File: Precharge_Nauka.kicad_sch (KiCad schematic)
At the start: 60 parts, among them Q1 C2M0280120D, Q2 C2M0280120D, Q3 C2M0280120D, Q4 2N7002, Q5 C2M0280120D, U32 LMV321

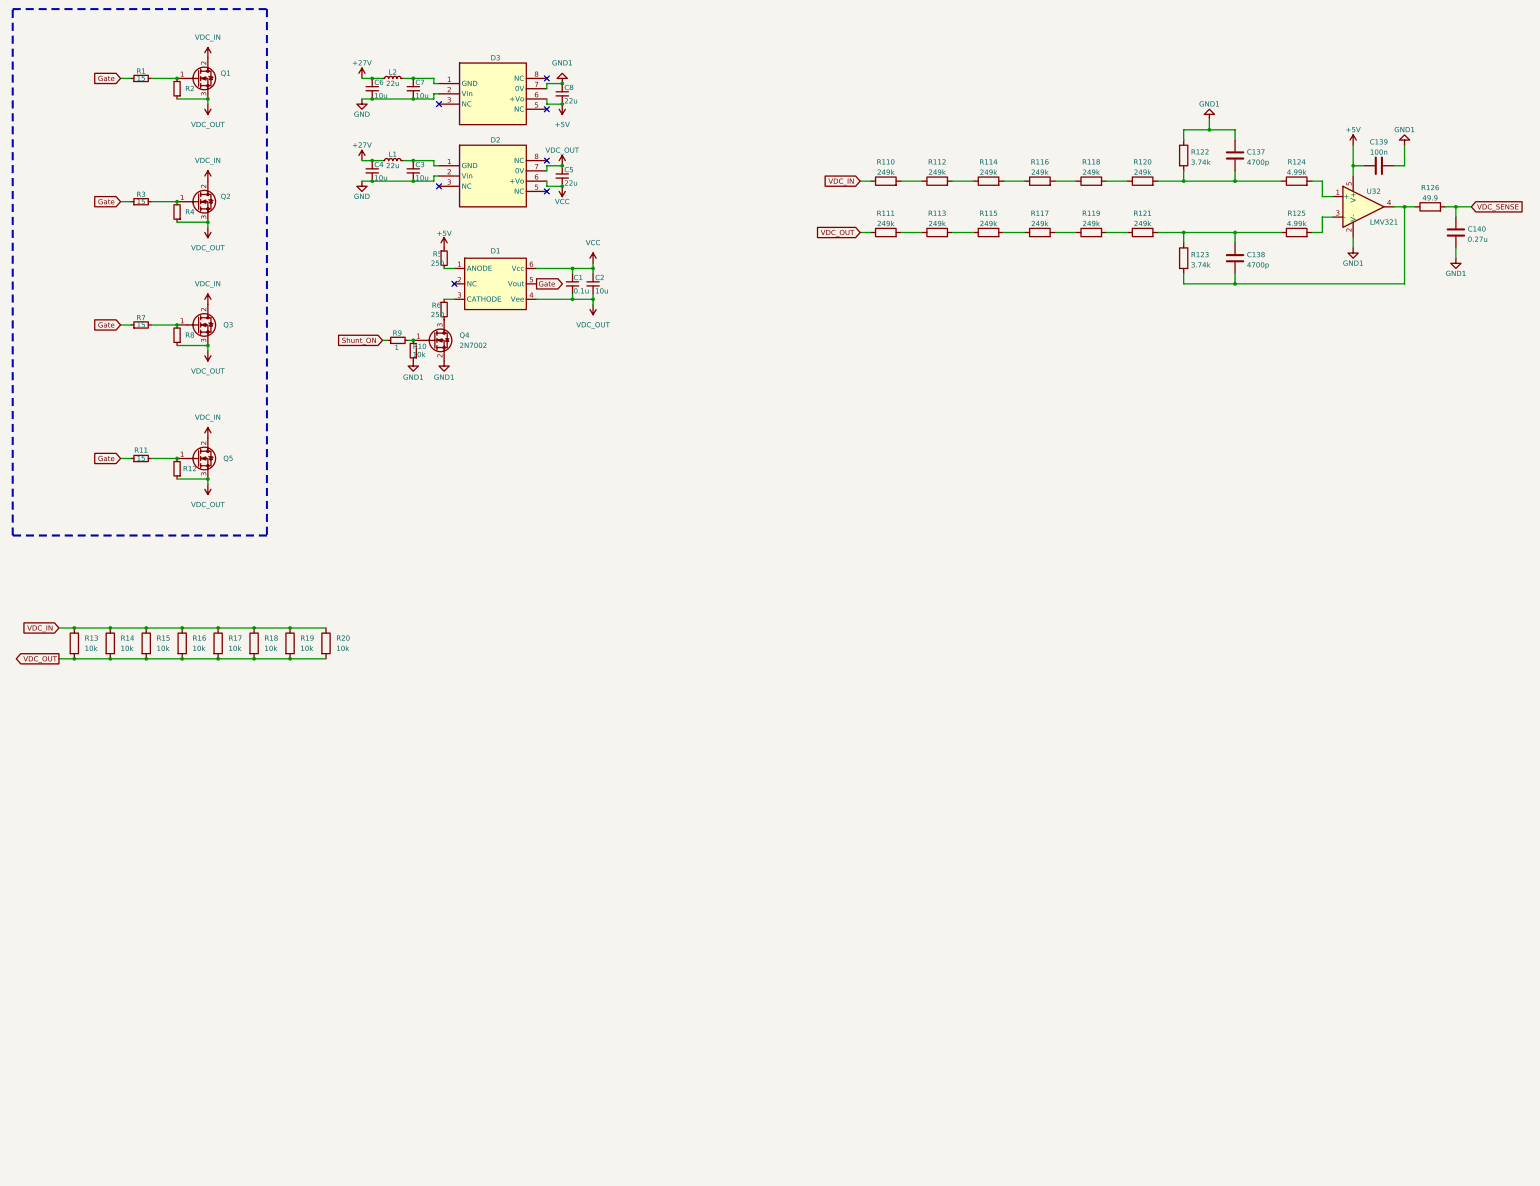
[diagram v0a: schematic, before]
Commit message: VER1.0: закончил основную схему и раскидал на плате
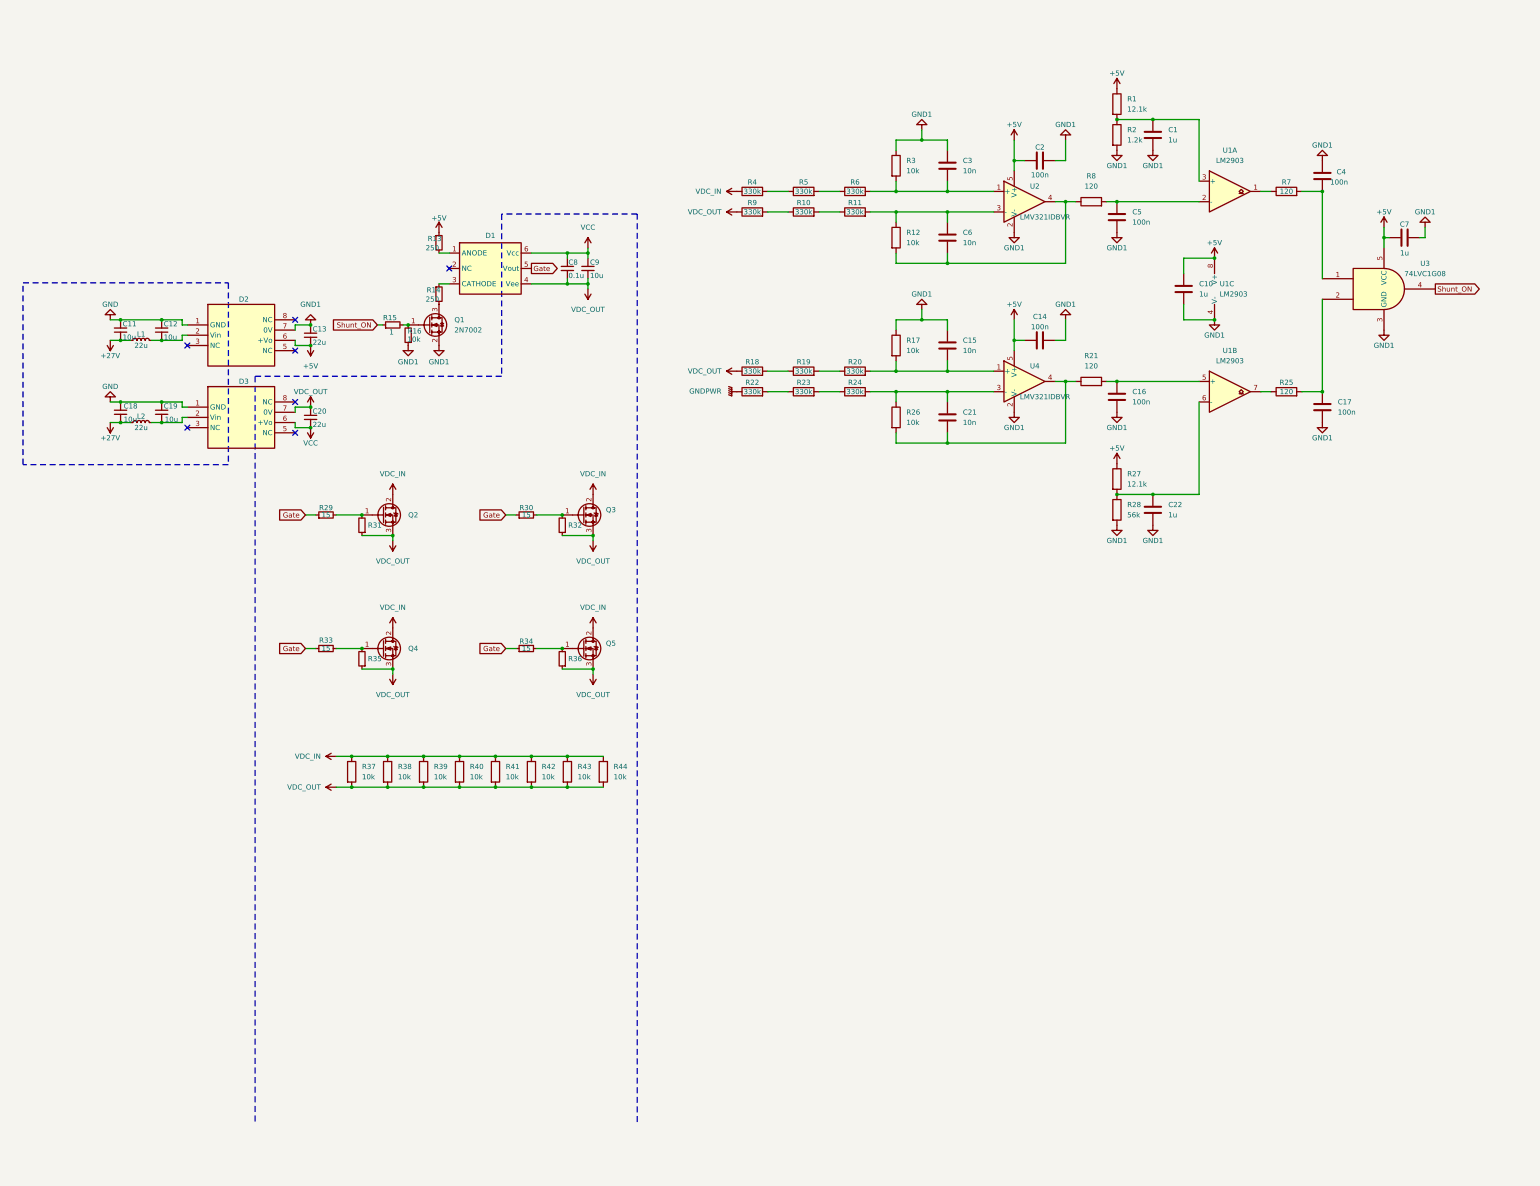
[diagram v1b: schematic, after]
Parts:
- removed R110, R111, R112, R113, R114, R115: 249k, Resistor_SMD:R_1206_3216Metric, symbol Device:R
- removed R124, R125: 4.99k, Resistor_SMD:R_0603_1608Metric, symbol Device:R
- added C1, C10, C22, C7: 1u, Capacitor_SMD:C_0805_2012Metric_Pad1.18x1.45mm_HandSolder, symbol Device:C
- added C14, C16, C17, C4: 100n, Capacitor_SMD:C_0805_2012Metric_Pad1.18x1.45mm_HandSolder, symbol Device:C
- added C15, C21: 10n, Capacitor_SMD:C_0805_2012Metric_Pad1.18x1.45mm_HandSolder, symbol Device:C
- added R1, R27: 12.1k, Resistor_SMD:R_0805_2012Metric_Pad1.20x1.40mm_HandSolder, symbol Device:R
- added R17, R26: 10k, Resistor_SMD:R_0805_2012Metric_Pad1.20x1.40mm_HandSolder, symbol Device:R
- added R18, R19, R20, R22, R23, R24: 330k, Resistor_SMD:R_1206_3216Metric, symbol Device:R
- added R2: 1.2k, Resistor_SMD:R_0805_2012Metric_Pad1.20x1.40mm_HandSolder, symbol Device:R
- added R21, R25, R7: 120, Resistor_SMD:R_0805_2012Metric_Pad1.20x1.40mm_HandSolder, symbol Device:R
- added R28: 56k, Resistor_SMD:R_0805_2012Metric_Pad1.20x1.40mm_HandSolder, symbol Device:R
- added U1: LM2903, Package_SO:SOP-8_3.76x4.96mm_P1.27mm, symbol Comparator:LM2903
- added U3: 74LVC1G08, Package_TO_SOT_SMD:SOT-23-5_HandSoldering, symbol 74xGxx:74LVC1G08
- added U4: LMV321IDBVR, Package_TO_SOT_SMD:SOT-23-5, symbol Amplifier_Operational:LMV321
- C2: renamed from C139; footprint Capacitor_SMD:C_0603_1608Metric -> Capacitor_SMD:C_0805_2012Metric_Pad1.18x1.45mm_HandSolder
- C3: renamed from C137; value 4700p -> 10n; footprint Capacitor_SMD:C_0603_1608Metric -> Capacitor_SMD:C_0805_2012Metric_Pad1.18x1.45mm_HandSolder
- C5: renamed from C140; value 0.27u -> 100n; footprint Capacitor_SMD:C_0603_1608Metric -> Capacitor_SMD:C_0805_2012Metric_Pad1.18x1.45mm_HandSolder
- C6: renamed from C138; value 4700p -> 10n; footprint Capacitor_SMD:C_0603_1608Metric -> Capacitor_SMD:C_0805_2012Metric_Pad1.18x1.45mm_HandSolder
- R10: renamed from R119; value 249k -> 330k
- R11: renamed from R121; value 249k -> 330k
- R12: renamed from R123; value 3.74k -> 10k; footprint Resistor_SMD:R_0603_1608Metric -> Resistor_SMD:R_0805_2012Metric_Pad1.20x1.40mm_HandSolder
- R3: renamed from R122; value 3.74k -> 10k; footprint Resistor_SMD:R_0603_1608Metric -> Resistor_SMD:R_0805_2012Metric_Pad1.20x1.40mm_HandSolder
- R4: renamed from R116; value 249k -> 330k
- R5: renamed from R118; value 249k -> 330k
- R6: renamed from R120; value 249k -> 330k
- R8: renamed from R126; value 49.9 -> 120; footprint Resistor_SMD:R_0603_1608Metric -> Resistor_SMD:R_0805_2012Metric_Pad1.20x1.40mm_HandSolder
- R9: renamed from R117; value 249k -> 330k
- U2: renamed from U32; value LMV321 -> LMV321IDBVR
- renumbered C6 to C11, C7 to C12, C8 to C13, C4 to C18, C3 to C19, C5 to C20, C1 to C8, C2 to C9, D3 to D2, D2 to D3, L2 to L1, L1 to L2, Q4 to Q1, Q3 to Q2, Q1 to Q3, Q5 to Q4, Q2 to Q5, R5 to R13, R6 to R14, R9 to R15, R10 to R16, R7 to R29, R1 to R30, R8 to R31, R2 to R32, R11 to R33, R3 to R34, R12 to R35, R4 to R36, R13 to R37, R14 to R38, R15 to R39, R16 to R40, R17 to R41, R18 to R42, R19 to R43, R20 to R44
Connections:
- net +27V: now also L1.2, L2.2; no longer L1.1, L2.1
- net +5V: now also C10.2, C14.1, C7.1, R1.1, R27.1, U1.8 (V+), U3.5 (VCC), U4.5 (V+)
- net GND: now also D2.1 (GND), D3.1 (GND); no longer D2.2 (Vin), D3.2 (Vin)
- net GND1: now also C1.2, C10.1, C14.2, C15.1, C16.2, C17.2, C22.2, C4.2, C7.2, R17.1, R2.2, R28.2, U1.4 (V-), U3.3 (GND), U4.2 (V-)
- net Shunt_ON: now also U3.4
- net VDC_IN: now also R4.1
- net VDC_OUT: now also R9.1, R18.1
- net at C3.2, R3.2, R6.2: now also U2.1 (+)
- net at C6.1, R11.2, R12.1: now also U2.3 (-)
- net VDC_SENSE: no longer names the net of C5.1, R8.2
- net VDC_SENSE: now also U1.2 (-)
- new net: C19.1, D3.2 (Vin), L2.1
- new net: R22.2, R23.1
- new net: C21.2, R21.1, R26.2, U4.4
- new net: C16.1, R21.2, U1.5 (+)
- new net: C15.2, R17.2, R20.2, U4.1 (+)
- new net: R18.2, R19.1
- new net: R7.1, U1.1
- new net: C4.1, R7.2, U3.1
- new net: R19.2, R20.1
- new net: C12.1, D2.2 (Vin), L1.1
- new net: R23.2, R24.1
- new net: C22.1, R27.2, R28.1, U1.6 (-)
- new net: C1.1, R1.2, R2.1, U1.3 (+)
- new net: C17.1, R25.2, U3.2
- new net: C21.1, R24.2, R26.1, U4.3 (-)
- new net: R25.1, U1.7
- new net GNDPWR: R22.1
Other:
- moved on the sheet: C11, C12, C13, C18, C19, C2, C20, C3, C5, C6, C8, C9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

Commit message: VER1.0: заменил цементные на 2512 резисторы
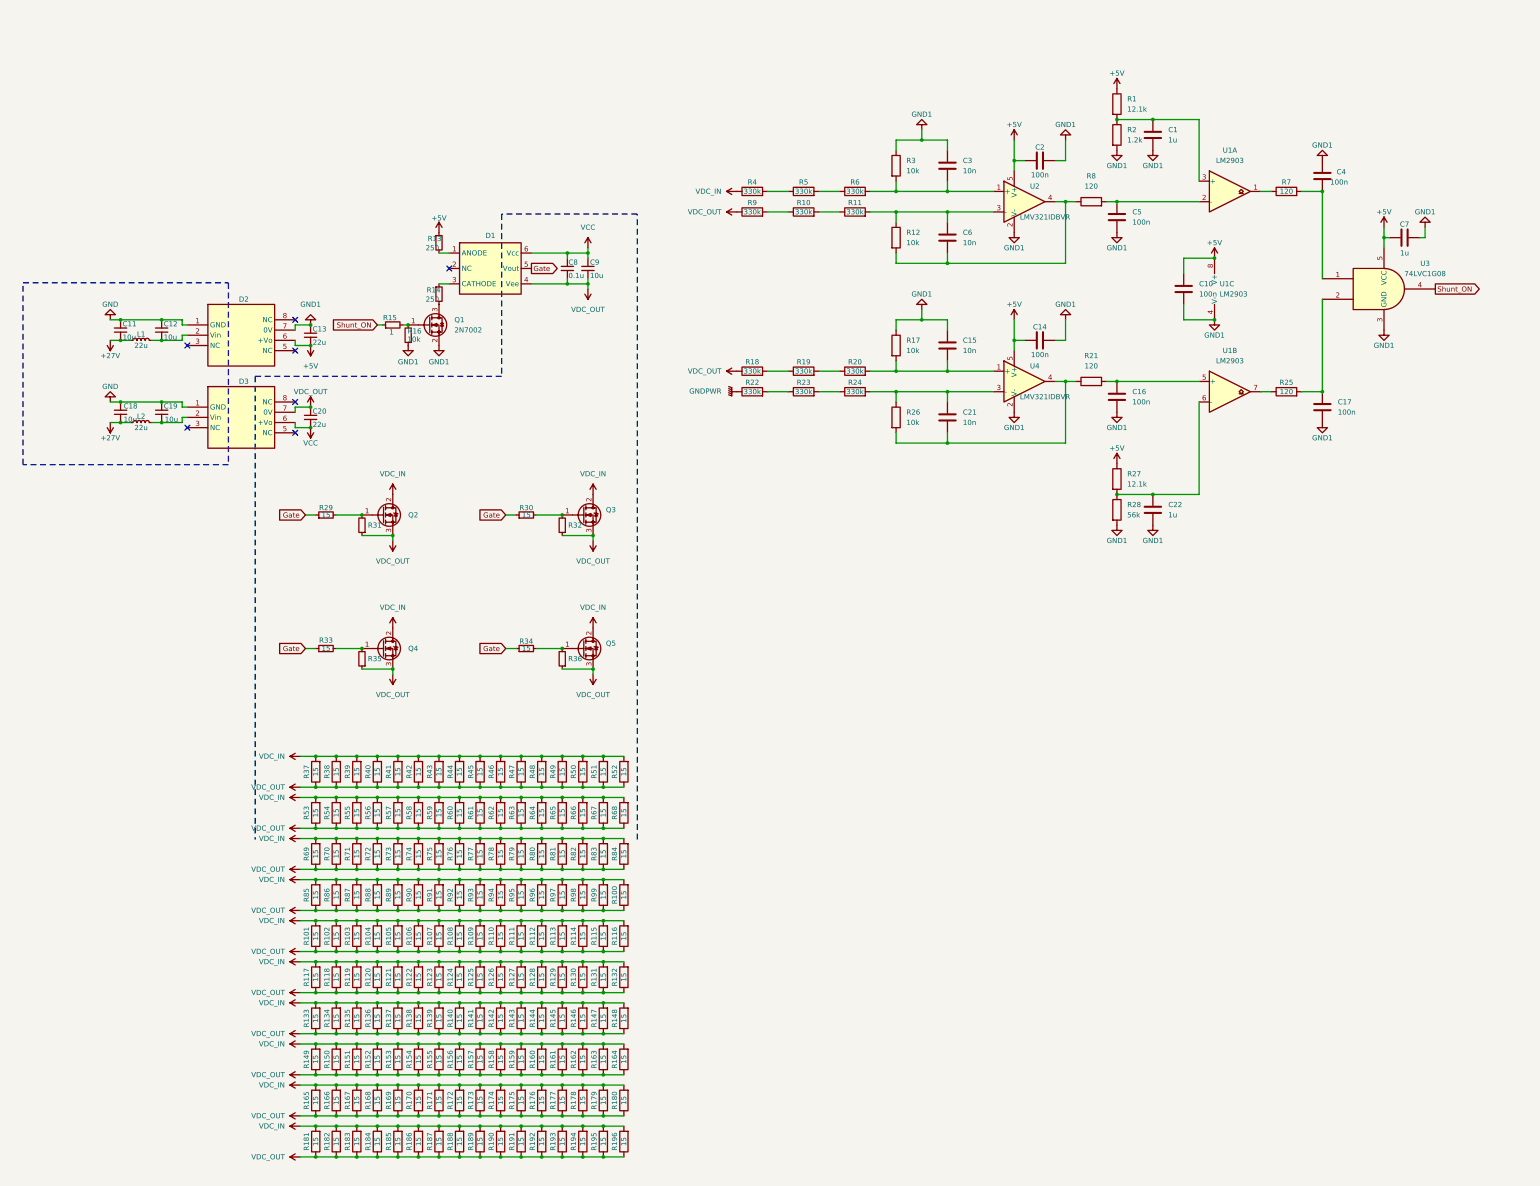
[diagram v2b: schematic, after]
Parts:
- added R100, R101, R102, R103, R104, R105, R106, R107, R108, R109, R110, R111, R112, R113, R114, R115, R116, R117, R118, R119, R120, R121, R122, R123, R124, R125, R126, R127, R128, R129, R130, R131, R132, R133, R134, R135, R136, R137, R138, R139, R140, R141, R142, R143, R144, R145, R146, R147, R148, R149, R150, R151, R152, R153, R154, R155, R156, R157, R158, R159, R160, R161, R162, R163, R164, R165, R166, R167, R168, R169, R170, R171, R172, R173, R174, R175, R176, R177, R178, R179, R180, R181, R182, R183, R184, R185, R186, R187, R188, R189, R190, R191, R192, R193, R194, R195, R196, R45, R46, R47, R48, R49, R50, R51, R52, R53, R54, R55, R56, R57, R58, R59, R60, R61, R62, R63, R64, R65, R66, R67, R68, R69, R70, R71, R72, R73, R74, R75, R76, R77, R78, R79, R80, R81, R82, R83, R84, R85, R86, R87, R88, R89, R90, R91, R92, R93, R94, R95, R96, R97, R98, R99: 15, Resistor_SMD:R_2512_6332Metric_Pad1.40x3.35mm_HandSolder, symbol Device:R
- C10: value 1u -> 100n
- R37, R38, R39, R40, R41, R42, R43, R44: value 10k -> 15; footprint Resistor_THT:R_Axial_Power_L60.0mm_W14.0mm_P66.04mm -> Resistor_SMD:R_2512_6332Metric_Pad1.40x3.35mm_HandSolder; Product Name SQP 20 Вт -> (none)
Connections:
- net VDC_IN: now also R37.2, R38.2, R39.2, R40.2, R41.2, R42.2, R43.2, R44.2, R100.2, R101.2, R102.2, R103.2, R104.2, R105.2, R106.2, R107.2, R108.2, R109.2, R110.2, R111.2, R112.2, R113.2, R114.2, R115.2, R116.2, R117.2, R118.2, R119.2, R120.2, R121.2, R122.2, R123.2, R124.2, R125.2, R126.2, R127.2, R128.2, R129.2, R130.2, R131.2, R132.2, R133.2, R134.2, R135.2, R136.2, R137.2, R138.2, R139.2, R140.2, R141.2, R142.2, R143.2, R144.2, R145.2, R146.2, R147.2, R148.2, R149.2, R150.2, R151.2, R152.2, R153.2, R154.2, R155.2, R156.2, R157.2, R158.2, R159.2, R160.2, R161.2, R162.2, R163.2, R164.2, R165.2, R166.2, R167.2, R168.2, R169.2, R170.2, R171.2, R172.2, R173.2, R174.2, R175.2, R176.2, R177.2, R178.2, R179.2, R180.2, R181.2, R182.2, R183.2, R184.2, R185.2, R186.2, R187.2, R188.2, R189.2, R190.2, R191.2, R192.2, R193.2, R194.2, R195.2, R196.2, R45.2, R46.2, R47.2, R48.2, R49.2, R50.2, R51.2, R52.2, R53.2, R54.2, R55.2, R56.2, R57.2, R58.2, R59.2, R60.2, R61.2, R62.2, R63.2, R64.2, R65.2, R66.2, R67.2, R68.2, R69.2, R70.2, R71.2, R72.2, R73.2, R74.2, R75.2, R76.2, R77.2, R78.2, R79.2, R80.2, R81.2, R82.2, R83.2, R84.2, R85.2, R86.2, R87.2, R88.2, R89.2, R90.2, R91.2, R92.2, R93.2, R94.2, R95.2, R96.2, R97.2, R98.2, R99.2; no longer R37.1, R38.1, R39.1, R40.1, R41.1, R42.1, R43.1, R44.1
- net VDC_OUT: now also R37.1, R38.1, R39.1, R40.1, R41.1, R42.1, R43.1, R44.1, R100.1, R101.1, R102.1, R103.1, R104.1, R105.1, R106.1, R107.1, R108.1, R109.1, R110.1, R111.1, R112.1, R113.1, R114.1, R115.1, R116.1, R117.1, R118.1, R119.1, R120.1, R121.1, R122.1, R123.1, R124.1, R125.1, R126.1, R127.1, R128.1, R129.1, R130.1, R131.1, R132.1, R133.1, R134.1, R135.1, R136.1, R137.1, R138.1, R139.1, R140.1, R141.1, R142.1, R143.1, R144.1, R145.1, R146.1, R147.1, R148.1, R149.1, R150.1, R151.1, R152.1, R153.1, R154.1, R155.1, R156.1, R157.1, R158.1, R159.1, R160.1, R161.1, R162.1, R163.1, R164.1, R165.1, R166.1, R167.1, R168.1, R169.1, R170.1, R171.1, R172.1, R173.1, R174.1, R175.1, R176.1, R177.1, R178.1, R179.1, R180.1, R181.1, R182.1, R183.1, R184.1, R185.1, R186.1, R187.1, R188.1, R189.1, R190.1, R191.1, R192.1, R193.1, R194.1, R195.1, R196.1, R45.1, R46.1, R47.1, R48.1, R49.1, R50.1, R51.1, R52.1, R53.1, R54.1, R55.1, R56.1, R57.1, R58.1, R59.1, R60.1, R61.1, R62.1, R63.1, R64.1, R65.1, R66.1, R67.1, R68.1, R69.1, R70.1, R71.1, R72.1, R73.1, R74.1, R75.1, R76.1, R77.1, R78.1, R79.1, R80.1, R81.1, R82.1, R83.1, R84.1, R85.1, R86.1, R87.1, R88.1, R89.1, R90.1, R91.1, R92.1, R93.1, R94.1, R95.1, R96.1, R97.1, R98.1, R99.1; no longer R37.2, R38.2, R39.2, R40.2, R41.2, R42.2, R43.2, R44.2

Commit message: VER1.0: надо проверить посадку новых транзисторов. Добавил обратную свзязь для компараторов
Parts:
- added J1: Conn_02x02_Top_Bottom, Connector_Molex:Molex_Micro-Fit_3.0_43045-0412_2x02_P3.00mm_Vertical, symbol Connector_Generic:Conn_02x02_Top_Bottom
- added R197, R198: 10k, Resistor_SMD:R_0805_2012Metric_Pad1.20x1.40mm_HandSolder, symbol Device:R
- D1: value ~ -> NSI6801
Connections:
- net +27V: now also J1.3 (Pin_3), J1.4 (Pin_4)
- net GND: now also J1.1 (Pin_1), J1.2 (Pin_2)
- net at C16.1, R21.2, U1.5 (+): now also R198.1
- net at R7.1, U1.1: now also R197.2
- net at C1.1, R1.2, R2.1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: now also R197.1
- net at R25.1, U1.7: now also R198.2

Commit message: VER1.0: добавил силовые стойки и развел силу
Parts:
- added J2, J3, J4: Conn_01x01, Connector_Power:SMD_15mm, symbol Connector_Generic:Conn_01x01
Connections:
- net GNDPWR: now also J4.1 (Pin_1)
- net VDC_IN: now also J2.1 (Pin_1)
- net VDC_OUT: now also J3.1 (Pin_1)

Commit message: VER1.0: увеличил фильтры компаратора, изменил схему предзарядных резисторов
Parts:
- C16, C17, C4, C5: value 100n -> 1u
- J4: footprint Connector_Power:SMD_15mm -> Connector_Power:SMD_8mm
- R100, R101, R102, R103, R104, R105, R106, R107, R108, R109, R110, R111, R112, R113, R114, R115, R116, R117, R118, R119, R120, R121, R122, R123, R124, R125, R126, R127, R128, R129, R130, R131, R132, R133, R134, R135, R136, R137, R138, R139, R140, R141, R142, R143, R144, R145, R146, R147, R148, R149, R150, R151, R152, R153, R154, R155, R156, R157, R158, R159, R160, R161, R162, R163, R164, R165, R166, R167, R168, R169, R170, R171, R172, R173, R174, R175, R176, R177, R178, R179, R180, R181, R182, R183, R184, R185, R186, R187, R188, R189, R190, R191, R192, R193, R194, R195, R196, R37, R38, R39, R40, R41, R42, R43, R44, R45, R46, R47, R48, R49, R50, R51, R52, R53, R54, R55, R56, R57, R58, R59, R60, R61, R62, R63, R64, R65, R66, R67, R68, R69, R70, R71, R72, R73, R74, R75, R76, R77, R78, R79, R80, R81, R82, R83, R84, R85, R86, R87, R88, R89, R90, R91, R92, R93, R94, R95, R96, R97, R98, R99: value 15 -> 8.2k
- R197, R198: value 10k -> 100k; now fitted
- R21, R8: value 120 -> 1k
- R25, R7: value 120 -> 10k
- U1: value LM2903 -> TS3702IDT
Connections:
- net VDC_IN: no longer R100.2, R102.2, R103.2, R104.2, R106.2, R107.2, R108.2, R110.2, R111.2, R112.2, R114.2, R115.2, R116.2, R118.2, R119.2, R120.2, R122.2, R123.2, R124.2, R126.2, R127.2, R128.2, R130.2, R131.2, R132.2, R134.2, R135.2, R136.2, R138.2, R139.2, R140.2, R142.2, R143.2, R144.2, R146.2, R147.2, R148.2, R150.2, R151.2, R152.2, R154.2, R155.2, R156.2, R158.2, R159.2, R160.2, R162.2, R163.2, R164.2, R166.2, R167.2, R168.2, R170.2, R171.2, R172.2, R174.2, R175.2, R176.2, R178.2, R179.2, R180.2, R182.2, R183.2, R184.2, R186.2, R187.2, R188.2, R190.2, R191.2, R192.2, R194.2, R195.2, R196.2, R37.2, R38.2, R39.2, R42.2, R43.2, R44.2, R46.2, R47.2, R48.2, R50.2, R51.2, R52.2, R54.2, R55.2, R56.2, R58.2, R59.2, R60.2, R62.2, R63.2, R64.2, R66.2, R67.2, R68.2, R70.2, R71.2, R72.2, R74.2, R75.2, R76.2, R78.2, R79.2, R80.2, R82.2, R83.2, R84.2, R86.2, R87.2, R88.2, R90.2, R91.2, R92.2, R94.2, R95.2, R96.2, R98.2, R99.2
- net VDC_OUT: now also R103.2, R107.2, R111.2, R115.2, R119.2, R123.2, R127.2, R131.2, R135.2, R139.2, R143.2, R147.2, R151.2, R155.2, R159.2, R163.2, R167.2, R171.2, R175.2, R179.2, R183.2, R187.2, R191.2, R195.2, R37.2, R43.2, R47.2, R51.2, R55.2, R59.2, R63.2, R67.2, R71.2, R75.2, R79.2, R83.2, R87.2, R91.2, R95.2, R99.2; no longer R100.1, R101.1, R102.1, R103.1, R104.1, R105.1, R106.1, R107.1, R108.1, R109.1, R110.1, R111.1, R112.1, R113.1, R114.1, R115.1, R116.1, R117.1, R118.1, R119.1, R120.1, R121.1, R122.1, R123.1, R124.1, R125.1, R126.1, R127.1, R128.1, R129.1, R130.1, R131.1, R132.1, R133.1, R134.1, R135.1, R136.1, R137.1, R138.1, R139.1, R140.1, R141.1, R142.1, R143.1, R144.1, R145.1, R146.1, R147.1, R148.1, R149.1, R150.1, R151.1, R152.1, R153.1, R154.1, R155.1, R156.1, R157.1, R158.1, R159.1, R160.1, R161.1, R162.1, R163.1, R164.1, R165.1, R166.1, R167.1, R168.1, R169.1, R170.1, R171.1, R172.1, R173.1, R174.1, R175.1, R176.1, R177.1, R178.1, R179.1, R180.1, R181.1, R182.1, R183.1, R184.1, R185.1, R186.1, R187.1, R188.1, R189.1, R190.1, R191.1, R192.1, R193.1, R194.1, R195.1, R196.1, R37.1, R38.1, R39.1, R40.1, R41.1, R42.1, R43.1, R44.1, R45.1, R46.1, R47.1, R48.1, R49.1, R50.1, R51.1, R52.1, R53.1, R54.1, R55.1, R56.1, R57.1, R58.1, R59.1, R60.1, R61.1, R62.1, R63.1, R64.1, R65.1, R66.1, R67.1, R68.1, R69.1, R70.1, R71.1, R72.1, R73.1, R74.1, R75.1, R76.1, R77.1, R78.1, R79.1, R80.1, R81.1, R82.1, R83.1, R84.1, R85.1, R86.1, R87.1, R88.1, R89.1, R90.1, R91.1, R92.1, R93.1, R94.1, R95.1, R96.1, R97.1, R98.1, R99.1
- new net: R97.1, R98.2
- new net: R42.1, R44.1
- new net: R41.1, R42.2
- new net: R166.1, R168.1
- new net: R165.1, R166.2
- new net: R81.1, R82.2
- new net: R191.1, R192.2
- new net: R162.1, R164.1
- new net: R161.1, R162.2
- new net: R106.1, R108.1
- new net: R105.1, R106.2
- new net: R174.1, R176.1
- new net: R173.1, R174.2
- new net: R111.1, R112.2
- new net: R82.1, R84.1
- new net: R83.1, R84.2
- new net: R135.1, R136.2
- new net: R151.1, R152.2
- new net: R190.1, R192.1
- new net: R54.1, R56.1
- new net: R55.1, R56.2
- new net: R182.1, R184.1
- new net: R183.1, R184.2
- new net: R78.1, R80.1
- new net: R79.1, R80.2
- new net: R158.1, R160.1
- new net: R157.1, R158.2
- new net: R70.1, R72.1
- new net: R71.1, R72.2
- new net: R86.1, R88.1
- new net: R87.1, R88.2
- new net: R178.1, R180.1
- new net: R177.1, R178.2
- new net: R110.1, R112.1
- new net: R73.1, R74.2
- new net: R141.1, R142.2
- new net: R181.1, R182.2
- new net: R154.1, R156.1
- new net: R153.1, R154.2
- new net: R169.1, R170.2
- new net: R130.1, R132.1
- new net: R131.1, R132.2
- new net: R145.1, R146.2
- new net: R186.1, R188.1
- new net: R187.1, R188.2
- new net: R74.1, R76.1
- new net: R155.1, R156.2
- new net: R167.1, R168.2
- new net: R50.1, R52.1
- new net: R49.1, R50.2
- new net: R57.1, R58.2
- new net: R46.1, R48.1
- new net: R47.1, R48.2
- new net: R138.1, R140.1
- new net: R137.1, R138.2
- new net: R129.1, R130.2
- new net: R150.1, R152.1
- new net: R149.1, R150.2
- new net: R118.1, R120.1
- new net: R117.1, R118.2
- new net: R146.1, R148.1
- new net: R77.1, R78.2
- new net: R126.1, R128.1
- new net: R125.1, R126.2
- new net: R107.1, R108.2
- new net: R58.1, R60.1
- new net: R194.1, R196.1
- new net: R193.1, R194.2
- new net: R163.1, R164.2
- new net: R75.1, R76.2
- new net: R67.1, R68.2
- new net: R94.1, R96.1
- new net: R95.1, R96.2
- new net: R102.1, R104.1
- new net: R103.1, R104.2
- new net: R159.1, R160.2
- new net: R69.1, R70.2
- new net: R93.1, R94.2
- new net: R113.1, R114.2
- new net: R38.1, R39.1
- new net: R37.1, R38.2
- new net: R59.1, R60.2
- new net: R45.1, R46.2
- new net: R195.1, R196.2
- new net: R115.1, R116.2
- new net: R171.1, R172.2
- new net: R100.2, R99.1
- new net: R51.1, R52.2
- new net: R109.1, R110.2
- new net: R122.1, R124.1
- new net: R121.1, R122.2
- new net: R53.1, R54.2
- new net: R185.1, R186.2
- new net: R61.1, R62.2
- new net: R43.1, R44.2
- new net: R101.1, R102.2
- new net: R170.1, R172.1
- new net: R39.2, R40.1
- new net: R179.1, R180.2
- new net: R139.1, R140.2
- new net: R90.1, R92.1
- new net: R91.1, R92.2
- new net: R114.1, R116.1
- new net: R66.1, R68.1
- new net: R65.1, R66.2
- new net: R147.1, R148.2
- new net: R89.1, R90.2
- new net: R123.1, R124.2
- new net: R189.1, R190.2
- new net: R85.1, R86.2
- new net: R62.1, R64.1
- new net: R127.1, R128.2
- new net: R175.1, R176.2
- new net: R134.1, R136.1
- new net: R133.1, R134.2
- new net: R100.1, R98.1
- new net: R142.1, R144.1
- new net: R143.1, R144.2
- new net: R119.1, R120.2
- new net: R63.1, R64.2
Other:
- moved on the sheet: J2, J3, J4, R37, R38, R39, R40

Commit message: VER1.0: изменил контур платы, сложно скомпоновать в размер
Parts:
- removed C8: 0.1u, Capacitor_SMD:C_1206_3216Metric_Pad1.33x1.80mm_HandSolder, symbol Device:C_Small
- removed J1: Conn_02x02_Top_Bottom, Connector_Molex:Molex_Micro-Fit_3.0_43045-0412_2x02_P3.00mm_Vertical, symbol Connector_Generic:Conn_02x02_Top_Bottom
- added J1: Conn_02x03_Top_Bottom, Connector_Molex:Molex_Micro-Fit_3.0_43045-0612_2x03_P3.00mm_Vertical, symbol Connector_Generic:Conn_02x03_Top_Bottom
- added Q6: 2N7002, Package_TO_SOT_SMD:SOT-23, symbol Transistor_FET:2N7002
- added R199, R200: 250, Resistor_SMD:R_0805_2012Metric_Pad1.20x1.40mm_HandSolder, symbol Device:R_Small
- added R201: 1, Resistor_SMD:R_0805_2012Metric_Pad1.20x1.40mm_HandSolder, symbol Device:R_Small
- added R202, R203: 10k, Resistor_SMD:R_0805_2012Metric_Pad1.20x1.40mm_HandSolder, symbol Device:R_Small
- added U5: PC817, Package_DIP:DIP-4_W7.62mm, symbol Isolator:PC817
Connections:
- net +27V: now also J1.4 (Pin_4), J1.5 (Pin_5), U5.4
- net +5V: now also R199.1
- net GND: now also J1.1 (Pin_1), J1.2 (Pin_2), R203.1
- net GND1: now also Q6.2 (S), R202.1
- net Shunt_ON: now also R201.1
- new net: R199.2, U5.1
- new net: R200.1, U5.2
- new net: Q6.1 (G), R201.2, R202.2
- new net: Q6.3 (D), R200.2
- new net Ready: J1.3 (Pin_3), J1.6 (Pin_6), R203.2, U5.3
